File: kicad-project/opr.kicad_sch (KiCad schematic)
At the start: 0 parts

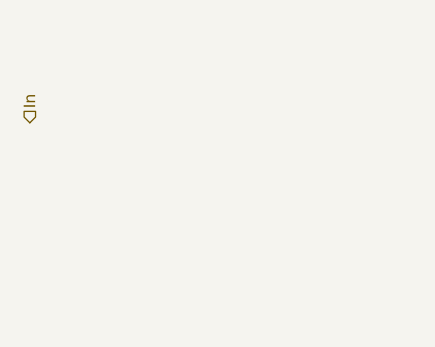
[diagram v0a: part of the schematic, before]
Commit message: update schematic
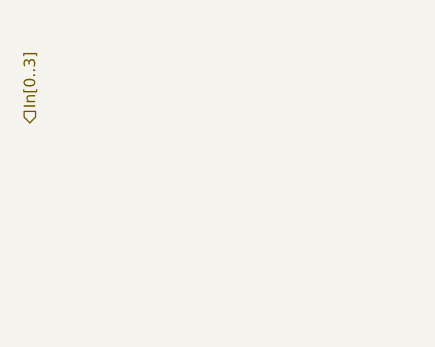
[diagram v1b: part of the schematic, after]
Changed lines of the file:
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@@
 (kicad_sch (version 20211123) (generator eeschema)
   (paper "A4")
-  (hierarchical_label "In" (shape input) (at 63.5 38.1 90)
+  (hierarchical_label "In[0..3]" (shape input) (at 63.5 38.1 90)
     (effects (font (size 1.27 1.27)) (justify left))
   )
